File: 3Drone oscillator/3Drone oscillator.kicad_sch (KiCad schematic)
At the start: 22 parts, among them J1 AudioJack2, Q1 2N3904, Q2 2N3904, Q3 2N3904, U1 TL071

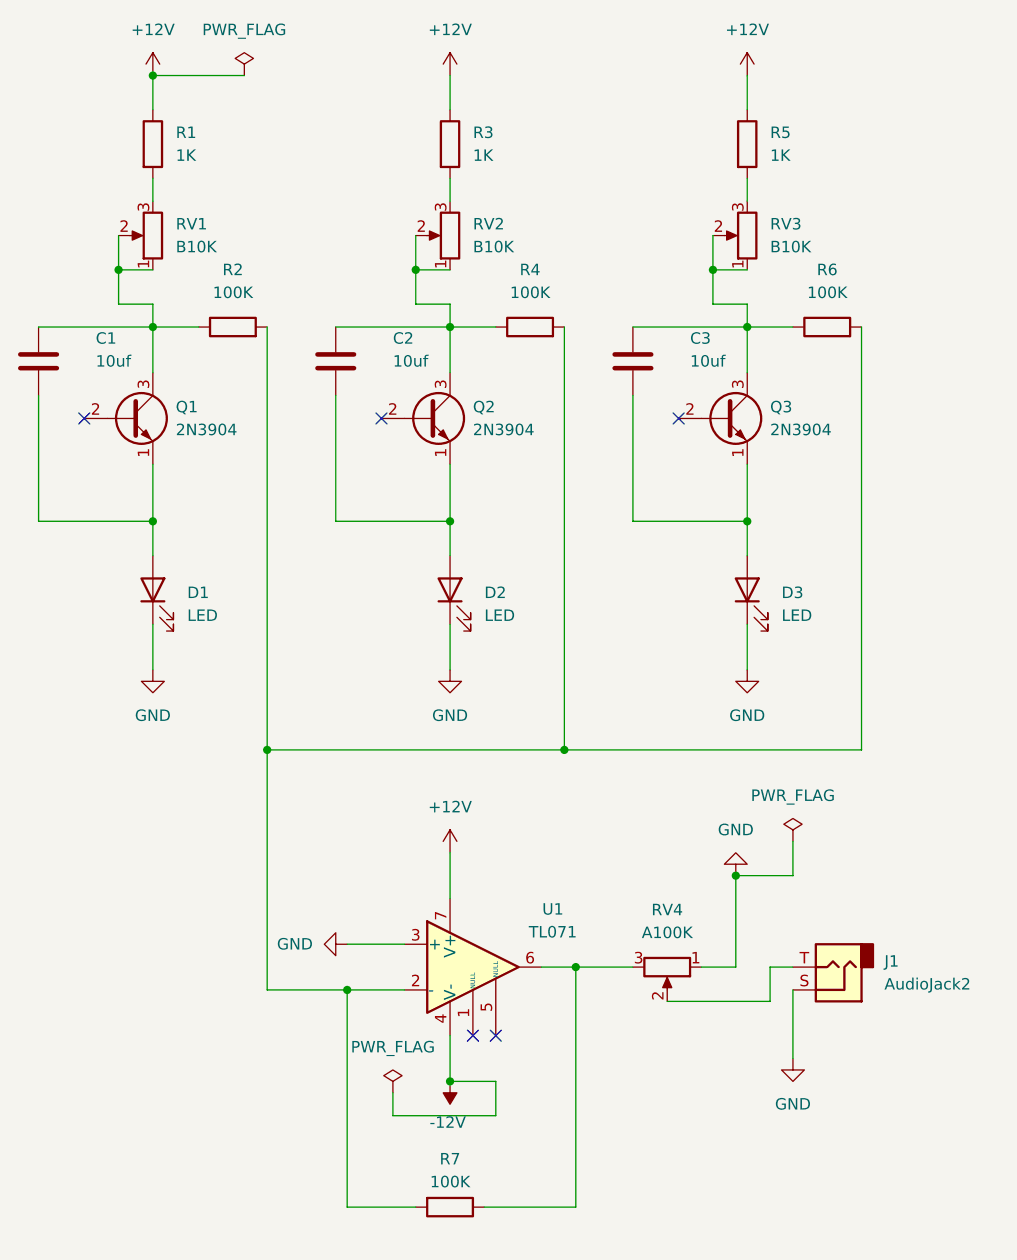
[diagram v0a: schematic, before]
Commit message: Added stripboard for triple avalanche
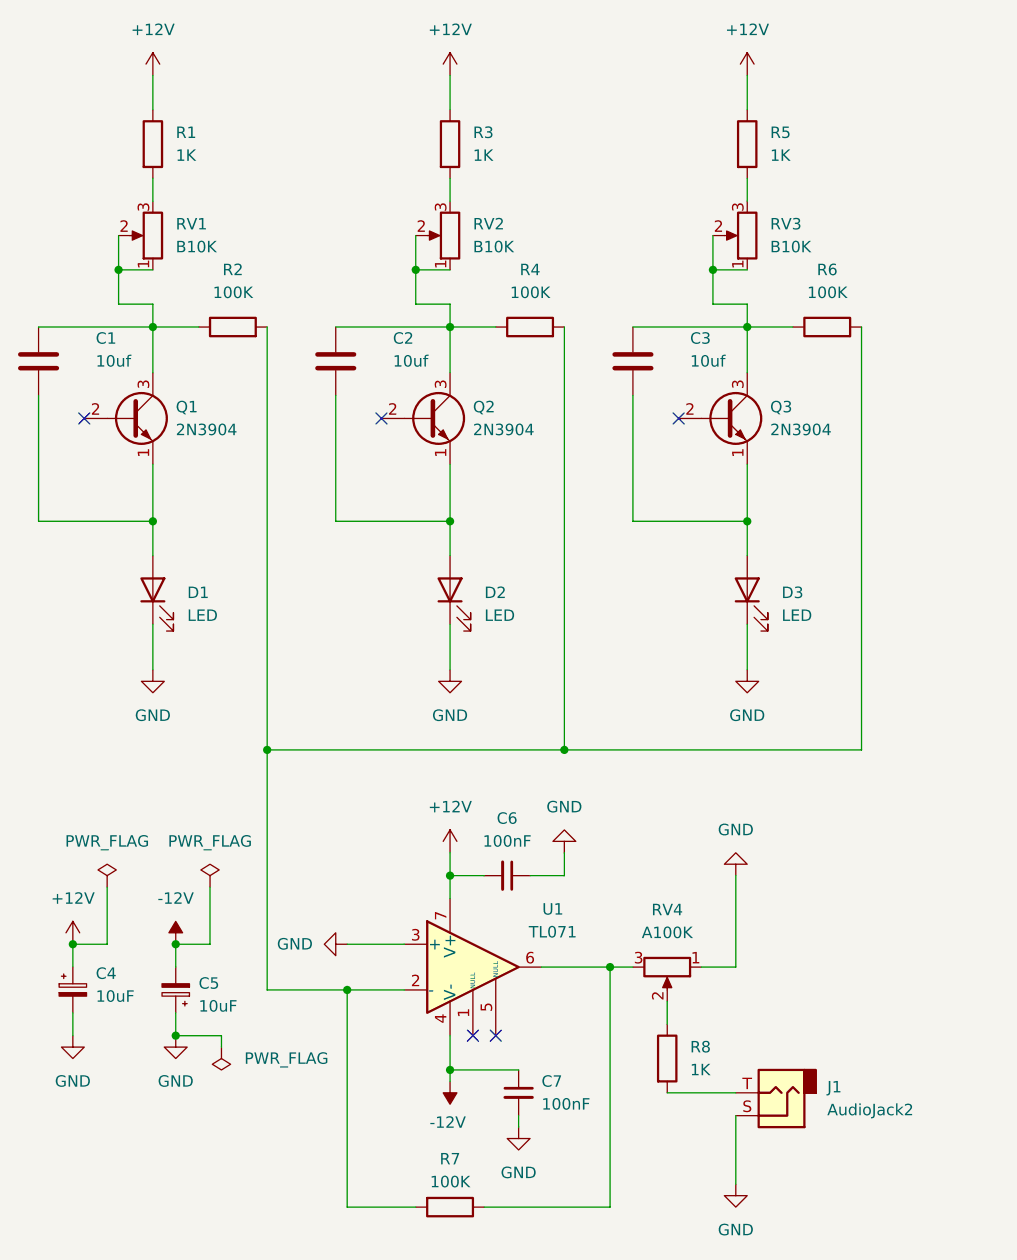
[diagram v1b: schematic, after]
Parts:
- added C4, C5: 10uF, symbol Device:C_Polarized_Small
- added C6, C7: 100nF, symbol Device:C_Small
- added R8: 1K, symbol Device:R
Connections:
- net +12V: now also C4.1, C6.2
- net -12V: now also C5.2, C7.1
- net GND: now also C4.2, C5.1, C6.1, C7.2
- net at RV4.2: now also R8.1; no longer J1.T
- new net: J1.T, R8.2
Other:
- moved on the sheet: J1
